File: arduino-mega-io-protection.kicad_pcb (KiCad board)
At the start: 4 copper layers, 150.1 x 72 mm, 207 parts, among them J101 CONN_01X02, J102 CONN_01X02, J103 CONN_01X02, J104 CONN_01X02, J105 CONN_01X02, J106 CONN_01X02, J107 CONN_01X02, J108 CONN_01X36, J109 CONN_01X10, J110 CONN_02X18, J111 CONN_01X08, J112 CONN_01X08, J113 CONN_01X08, J114 CONN_01X08, J115 CONN_01X08, J116 CONN_01X02, J117 CONN_01X02, J118 CONN_01X02, P301 J1B1211CCD, SW301 SW_Push, U201 MOCD217M, U202 MOCD217M, U203 MOCD217M, U204 MOCD217M, U205 MOCD217M, U206 MOCD217M, U209 MOCD217M, U210 MOCD217M, U211 MOCD217M, U212 MOCD217M, U213 MOCD217M, U214 MOCD217M, U215 MOCD217M, U216 MOCD217M, U217 MOCD217M, U218 MOCD217M, U219 MOCD217M, U220 MOCD217M, U221 MOCD217M, U222 MOCD217M, U223 MOCD217M, U224 MOCD217M, U225 MOCD217M, U301 W5500, Y301 25Mhz

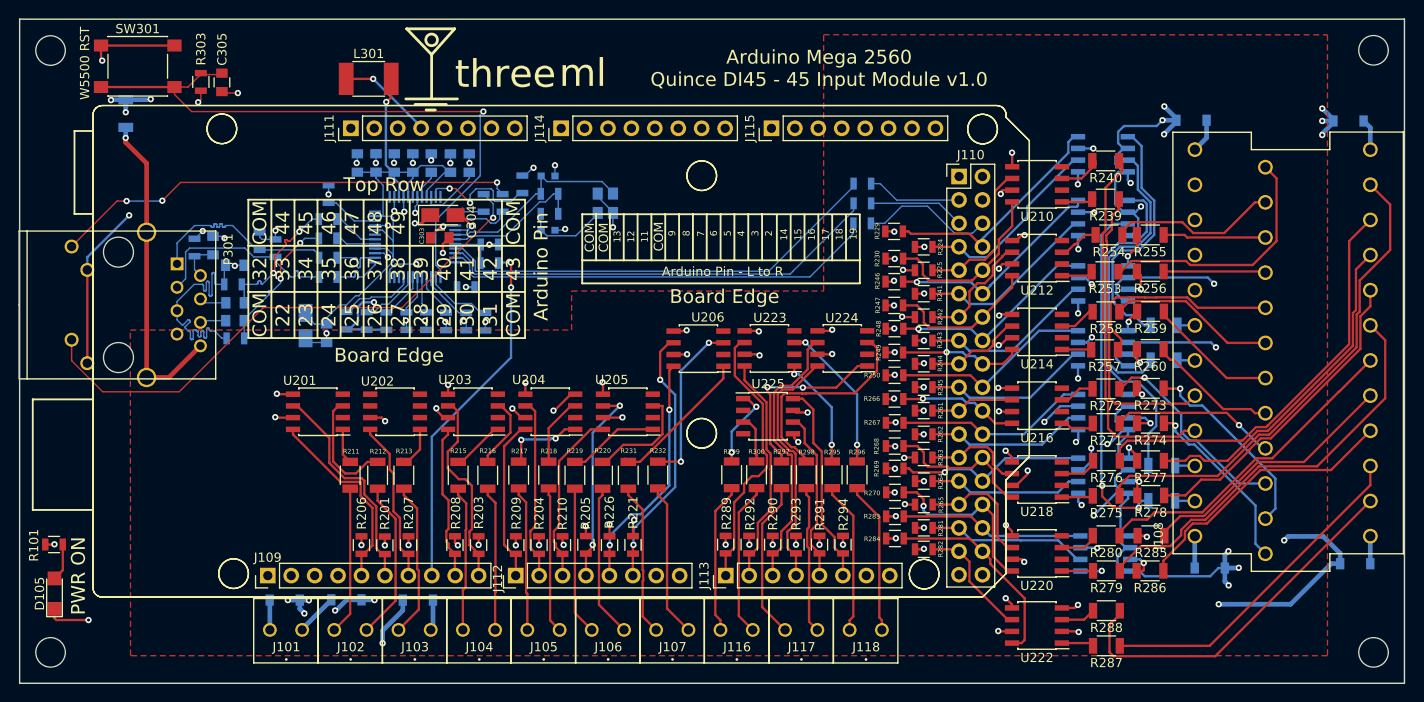
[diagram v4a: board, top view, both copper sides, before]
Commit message: updating schematic and library to use a Phoenix header for the 1x20
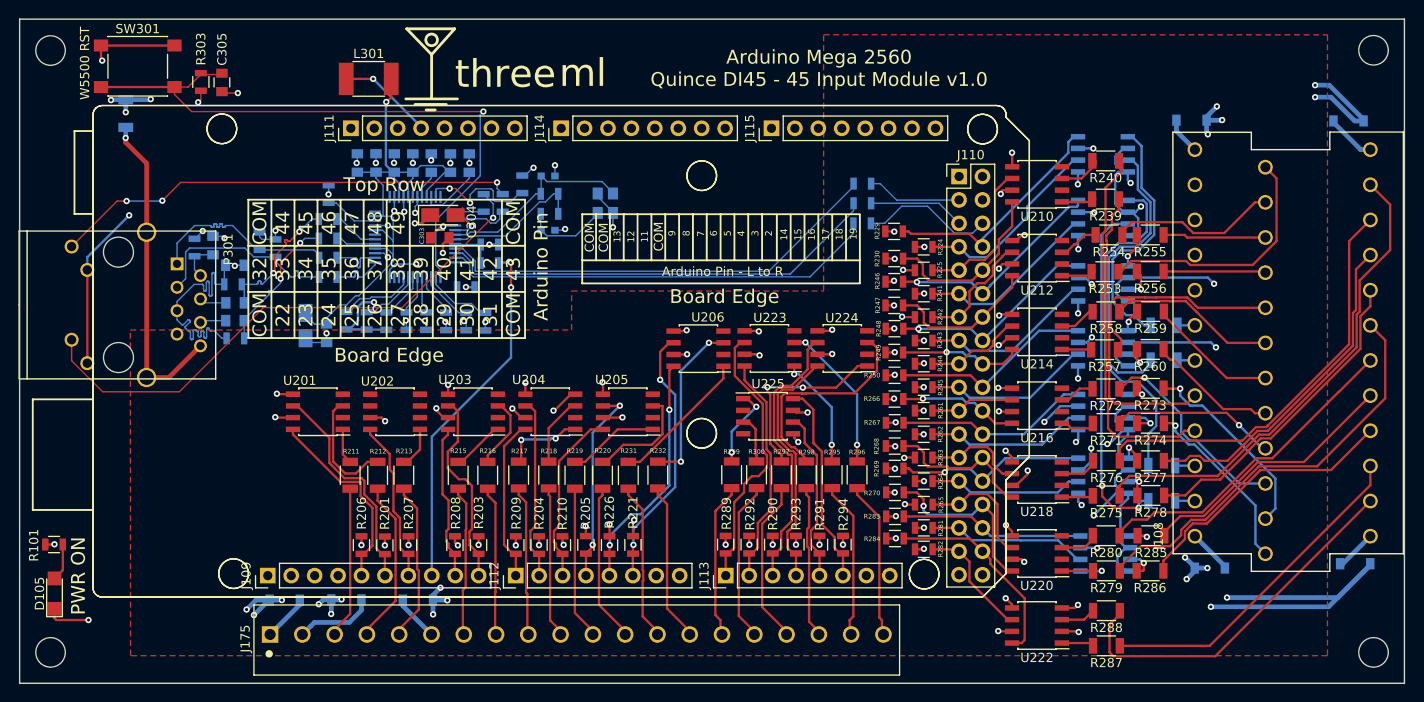
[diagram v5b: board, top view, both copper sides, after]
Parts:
- removed J101, J102, J103, J104, J105, J106, J107, J116, J117, J118: CONN_01X02, 3ML_Footprint_Library:Wurth_691103010002
- added J175: Conn_01x20, 3ML_Conn_Headers:Phoenix-1x20-1709678, F.Cu at (101.6, 140.5)
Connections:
- D101 pad 1: GND -> Net-(D101-Pad1)
- D101 pad 2: Net-(D101-Pad2) -> GND
- D102 pad 1: GND -> Net-(D102-Pad1)
- D102 pad 2: Net-(D102-Pad2) -> GND
- D103 pad 1: GND -> Net-(D103-Pad1)
- D103 pad 2: Net-(D103-Pad2) -> GND
- D104 pad 1: GND -> Net-(D104-Pad1)
- D104 pad 2: Net-(D104-Pad2) -> GND
- D106 pad 1: GND -> Net-(D106-Pad1)
- D106 pad 2: Net-(D106-Pad2) -> GND
- D107 pad 1: GND -> Net-(D107-Pad1)
- D107 pad 2: Net-(D107-Pad2) -> GND
- D108 pad 1: GND -> Net-(D108-Pad1)
- D108 pad 2: Net-(D108-Pad2) -> GND
- J108 pad 1: Net-(D108-Pad2) -> Net-(D108-Pad1)
- J108 pad 12: Net-(D107-Pad2) -> Net-(D107-Pad1)
- J108 pad 25: Net-(D106-Pad2) -> Net-(D106-Pad1)
- J108 pad 36: Net-(D104-Pad2) -> Net-(D104-Pad1)
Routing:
- net Net-(D103-Pad1): track 0.00 -> 8.71 mm
- net Net-(D107-Pad1): track 0.00 -> 5.54 mm
- net Net-(D102-Pad1): track 0.00 -> 5.10 mm
- net Net-(D101-Pad1): track 0.00 -> 5.06 mm
- net Net-(D106-Pad1): track 0.00 -> 4.83 mm
- net Net-(D103-Pad2): track 4.58 -> 0.00 mm
- net Net-(D108-Pad1): track 0.00 -> 4.52 mm
- net Net-(D104-Pad1): track 0.00 -> 4.35 mm
- net Net-(D104-Pad2): track 3.71 -> 0.00 mm
- net Net-(D106-Pad2): track 3.46 -> 0.00 mm
- net Net-(D107-Pad2): track 3.41 -> 0.00 mm
- net Net-(D102-Pad2): track 3.35 -> 0.00 mm
- net Net-(D101-Pad2): track 3.25 -> 0.00 mm
- net Net-(D108-Pad2): track 2.98 -> 0.00 mm
- net GND: track 160.0 -> 162.9 mm, vias 26 -> 28

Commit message: removing unnecessary diodes
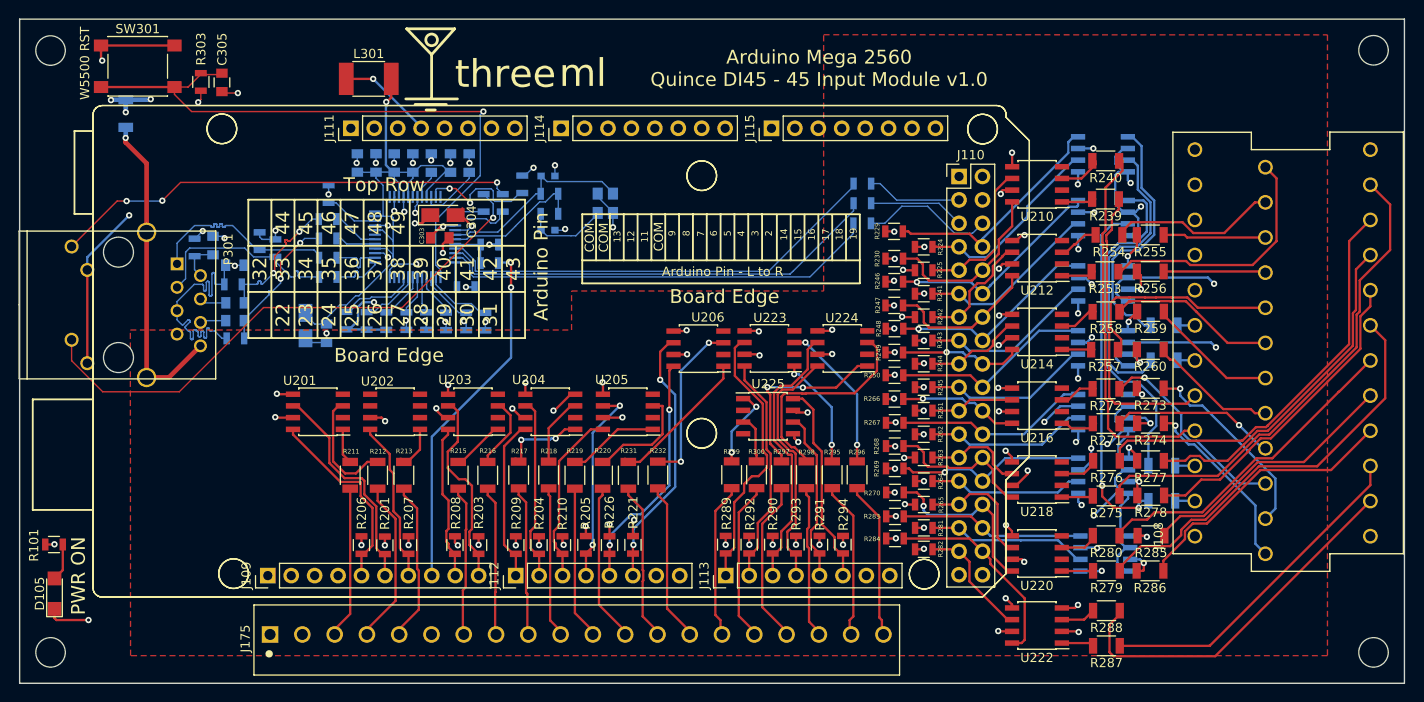
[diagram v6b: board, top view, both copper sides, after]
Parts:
- removed D101, D102, D103, D104, D106, D107, D108: 0.5W, Diodes_SMD:SOD-123
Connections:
- J108 pad 1: Net-(D108-Pad1) -> (no net)
- J108 pad 12: Net-(D107-Pad1) -> (no net)
- J108 pad 25: Net-(D106-Pad1) -> (no net)
- J108 pad 36: Net-(D104-Pad1) -> (no net)
- J175 pad 1: Net-(D101-Pad1) -> GND
- J175 pad 2: Net-(D103-Pad1) -> GND
- J175 pad 6: Net-(D102-Pad1) -> GND
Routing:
- net GND: track 162.9 -> 87.9 mm, vias 28 -> 9
- net Net-(D103-Pad1): track 8.71 -> 0.00 mm
- net Net-(D107-Pad1): track 5.54 -> 0.00 mm
- net Net-(D102-Pad1): track 5.10 -> 0.00 mm
- net Net-(D101-Pad1): track 5.06 -> 0.00 mm
- net Net-(D106-Pad1): track 4.83 -> 0.00 mm
- net Net-(D108-Pad1): track 4.52 -> 0.00 mm
- net Net-(D104-Pad1): track 4.35 -> 0.00 mm
